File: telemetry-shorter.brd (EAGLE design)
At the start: 69.8 x 22.9 mm, 60 parts, among them SW1 B3U-1000P-2P-SMD, U1 ATSAMD21G18_QFN, U2 SPX3819M5-L-3-0, U3 MCP73831T-2ACI/OT, U4 MPU-9250, U5 SIM868, U6 BMP280, X1 JSTPH, X2 32.768, X3 ZX62-B-5PA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

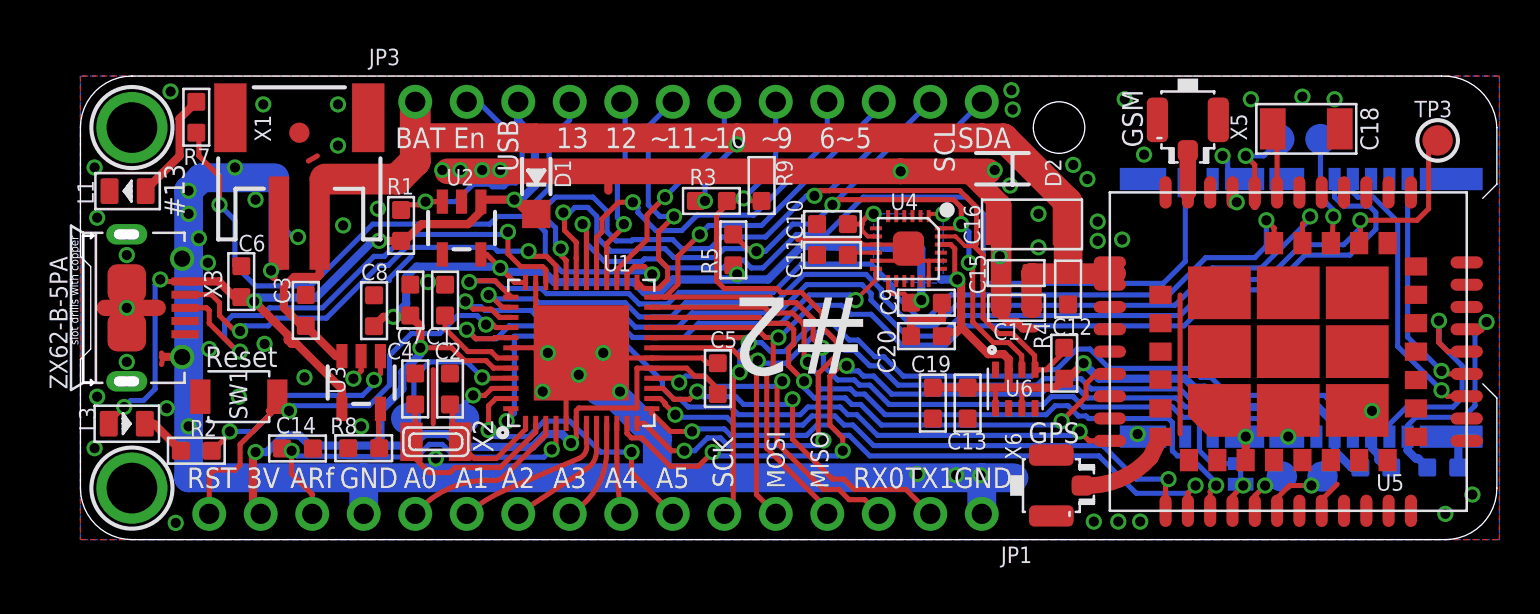
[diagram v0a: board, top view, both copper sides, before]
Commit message: Connected GPS_EN to 2V8 by jumper
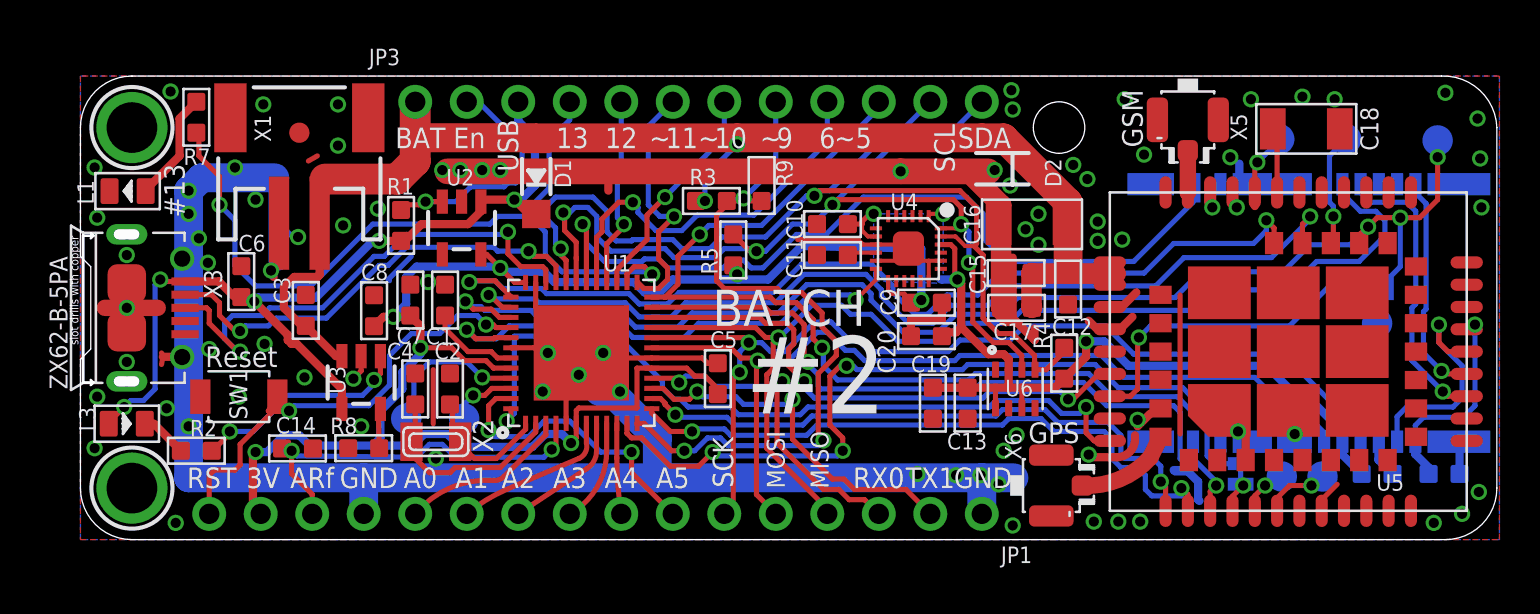
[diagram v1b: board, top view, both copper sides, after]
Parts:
- added JP4: JUMPER-PAD-2-NC_BY_TRACE, SparkFun-Passives:PAD-JUMPER-2-NC_BY_TRACE_YES_SILK
- added TP7: (no value), microbuilder:TESTPOINT_ROUND_1.5MM
- moved TP4 1.27 mm to (62.4, 19.7)
- moved X4 0.46 mm to (60.6, 11.2)
- moved C28 0.32 mm to (63.9, 3.24)
- moved C21 0.32 mm to (67.2, 3.24)
- flipped TP3 to the bottom
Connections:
- removed net VDD_EXT(2.8VOUT): U5.40_
- new net VDD_EXT_2V8: JP4.2, TP7.P$1, U5.40_
- net GPS_EN: now also JP4.1
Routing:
- net VDD_EXT_2V8: track 0.00 -> 18.3 mm, vias 0 -> 1
- net GND: track 171.0 -> 183.7 mm, vias 73 -> 83
- net D7/SD_DET: track 43.9 -> 40.2 mm
- net GPS_EN: track 60.7 -> 63.4 mm, vias 2 -> 4
- net +3V: track 125.6 -> 127.0 mm
- net SIM_VDD: track 11.8 -> 10.5 mm
- net PWRKEY: track 27.8 -> 26.6 mm
- net STATUS: track 37.2 -> 38.3 mm
- net RF_SYNC: track 4.69 -> 3.80 mm
- net D3/RX2/GSM_TX: track 29.2 -> 30.0 mm
- net D4/TX2/GSM_RX: track 30.8 -> 31.4 mm
- net TX5/GPS_RX: track 48.3 -> 47.8 mm
- net GPS_1PPS: track 5.43 -> 5.93 mm
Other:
- outline, holes or cut-outs redrawn
- board text added: "BATCH"
